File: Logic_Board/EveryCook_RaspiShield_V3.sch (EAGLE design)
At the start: 98 parts, among them IC1 LM386MM-1, IC2 ATMEGA644A, Q1 8 MHz, Q2 BSP372, Q3 BSP372, T2 ZDT6790, U1 AD7794BRUZ, U4 78M05, U7 CJ1117-3.3

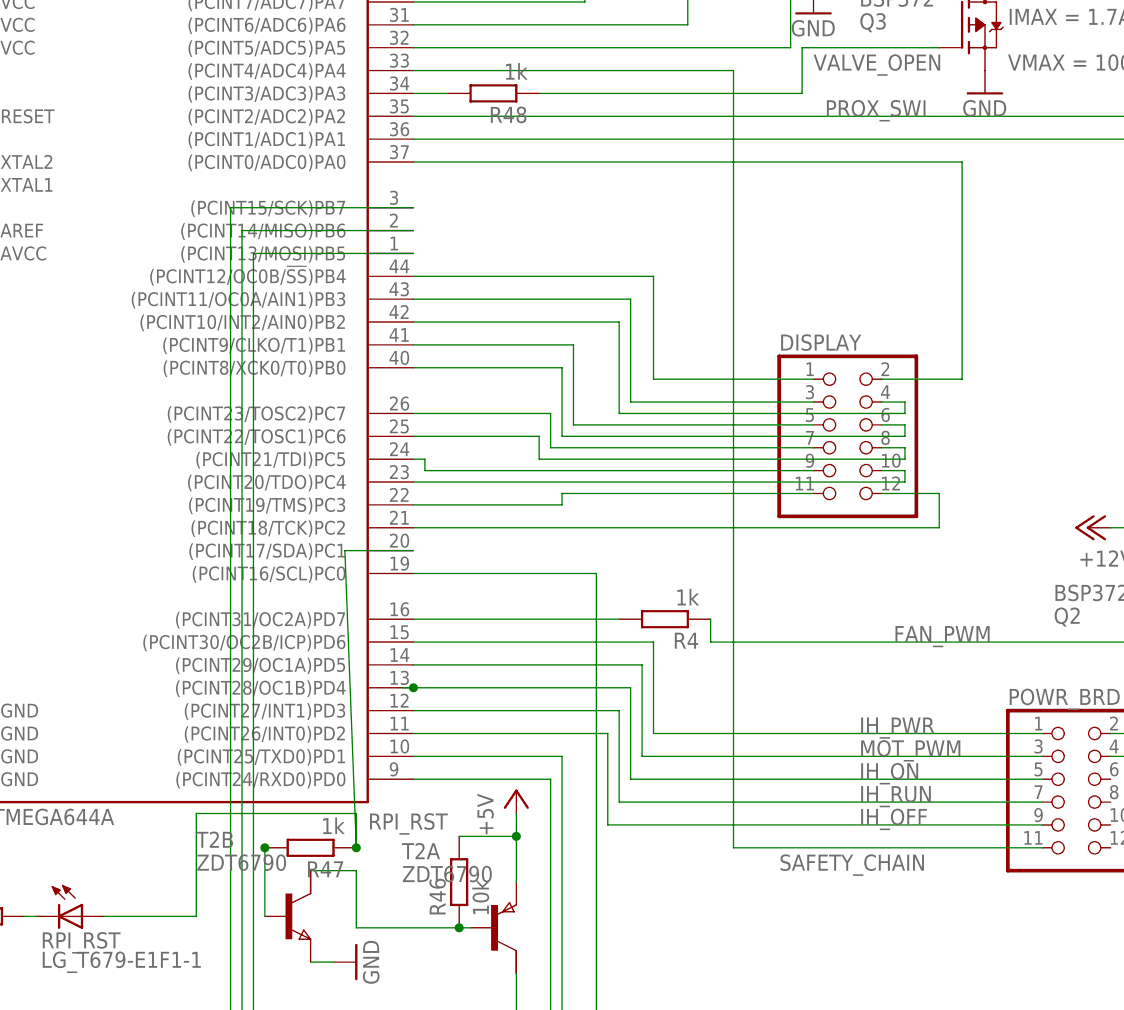
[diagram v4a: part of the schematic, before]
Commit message: Re-routed a display pin to have the whole display on ports B and C. Safety chain board layouted.
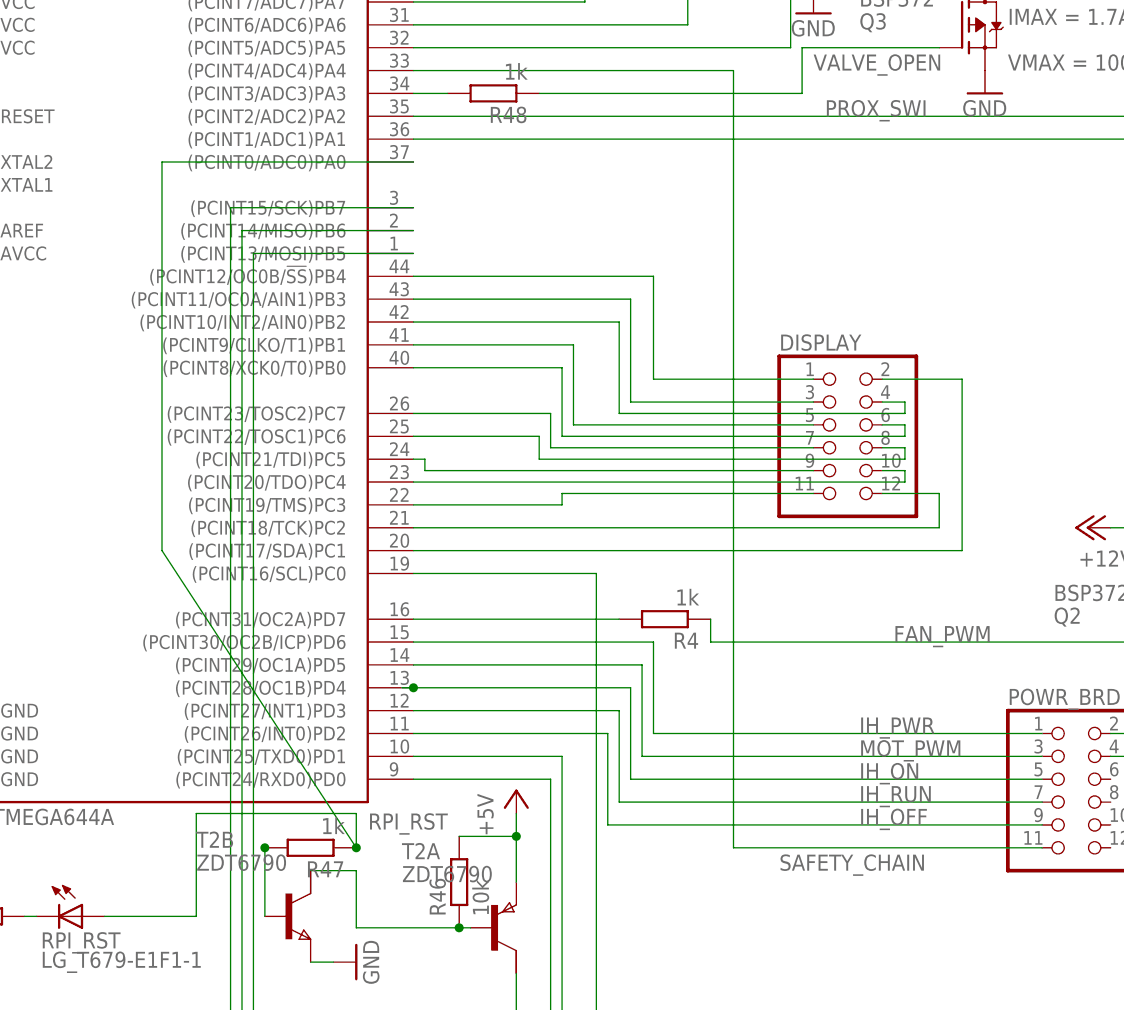
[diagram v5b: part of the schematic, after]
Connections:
- removed net N$49: DISPLAY.2, IC2.(PCINT0/ADC0)PA0
- new net N$1: DISPLAY.2, IC2.(PCINT17/SDA)PC1
- net RPI_RST: now also IC2.(PCINT0/ADC0)PA0; no longer IC2.(PCINT17/SDA)PC1
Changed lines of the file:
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@@
 <setting verticaltext="up"/>
 </settings>
-<grid distance="0.05" unitdist="inch" unit="inch" style="lines" multiple="1" display="no" altdistance="0.025" altunitdist="inch" altunit="inch"/>
+<grid distance="0.05" unitdist="inch" unit="inch" style="lines" multiple="1" display="no" altdistance="0.01" altunitdist="inch" altunit="inch"/>
 <layers>
 <layer number="1" name="Top" color="4" fill="1" visible="no" active="no"/>
@@
 </segment>
 </net>
-<net name="N$49" class="0">
-<segment>
-<pinref part="DISPLAY" gate="A" pin="2"/>
-<wire x1="158.75" y1="146.05" x2="167.64" y2="146.05" width="0.1524" layer="91"/>
-<wire x1="167.64" y1="146.05" x2="167.64" y2="170.18" width="0.1524" layer="91"/>
-<pinref part="IC2" gate="G$1" pin="(PCINT0/ADC0)PA0"/>
-<wire x1="167.64" y1="170.18" x2="106.68" y2="170.18" width="0.1524" layer="91"/>
-</segment>
-</net>
 <net name="FAN_PWM" class="0">
 <segment>
@@
 <net name="RPI_RST" class="0">
 <segment>
-<wire x1="100.33" y1="93.98" x2="99.06" y2="127" width="0.1524" layer="91"/>
-<pinref part="IC2" gate="G$1" pin="(PCINT17/SDA)PC1"/>
-<wire x1="99.06" y1="127" x2="106.68" y2="127" width="0.1524" layer="91"/>
+<wire x1="100.33" y1="93.98" x2="78.74" y2="127" width="0.1524" layer="91"/>
 <pinref part="R47" gate="G$1" pin="1"/>
 <junction x="100.33" y="93.98"/>
@@
 <wire x1="82.55" y1="97.79" x2="100.33" y2="97.79" width="0.1524" layer="91"/>
 <wire x1="100.33" y1="97.79" x2="100.33" y2="93.98" width="0.1524" layer="91"/>
+<wire x1="78.74" y1="127" x2="78.74" y2="170.18" width="0.1524" layer="91"/>
+<pinref part="IC2" gate="G$1" pin="(PCINT0/ADC0)PA0"/>
+<wire x1="78.74" y1="170.18" x2="106.68" y2="170.18" width="0.1524" layer="91"/>
 </segment>
 </net>
@@
 </segment>
 </net>
+<net name="N$1" class="0">
+<segment>
+<pinref part="IC2" gate="G$1" pin="(PCINT17/SDA)PC1"/>
+<wire x1="106.68" y1="127" x2="167.64" y2="127" width="0.1524" layer="91"/>
+<wire x1="167.64" y1="127" x2="167.64" y2="146.05" width="0.1524" layer="91"/>
+<pinref part="DISPLAY" gate="A" pin="2"/>
+<wire x1="158.75" y1="146.05" x2="167.64" y2="146.05" width="0.1524" layer="91"/>
+</segment>
+</net>
